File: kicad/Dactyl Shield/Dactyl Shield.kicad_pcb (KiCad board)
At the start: 4 copper layers, 99.4 x 91.3 mm, 130 parts, among them J201 JST, J202 Split, J203 Column, J205 Foot, J206 Row, J207 Display, J208 Vic, J209 ResA, J210 Thumb_row, J211 Thumb_upper, J212 ResB, J213 Thumb_lower, J301 JST, J302 Split, J303 Column, J305 Foot, J306 Row, J307 Display, J308 Vic, J309 ResA, J310 Thumb_row, J311 Thumb_upper, J312 ResB, J313 Thumb_lower, Q201 AO3400A, Q301 AO3400A, SW201 Battery, SW202 Reset, SW203 LED, SW301 Battery, SW302 Reset, SW303 LED, U201 SRV05-4, U202 Nice!Nano/2040, U301 SRV05-4, U302 Nice!Nano/2040

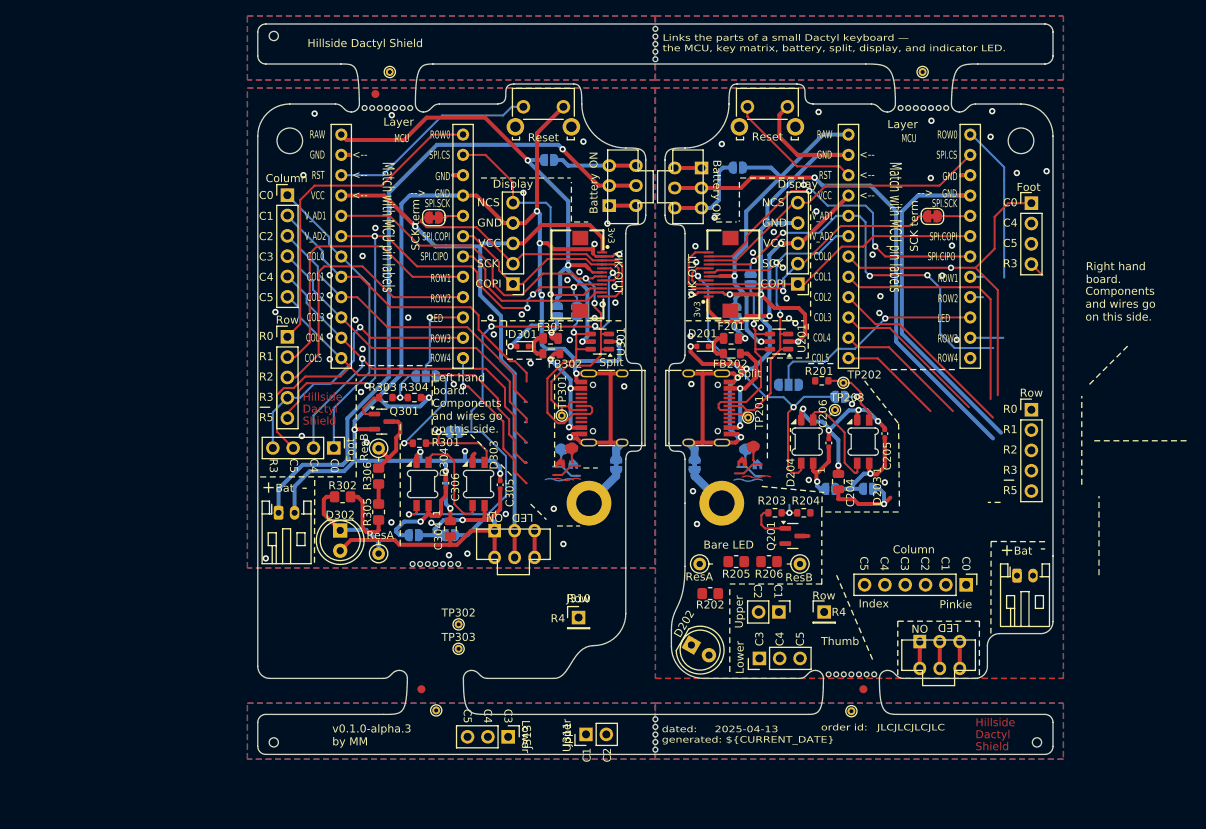
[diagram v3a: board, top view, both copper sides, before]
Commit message: feat: right side wired and seems good
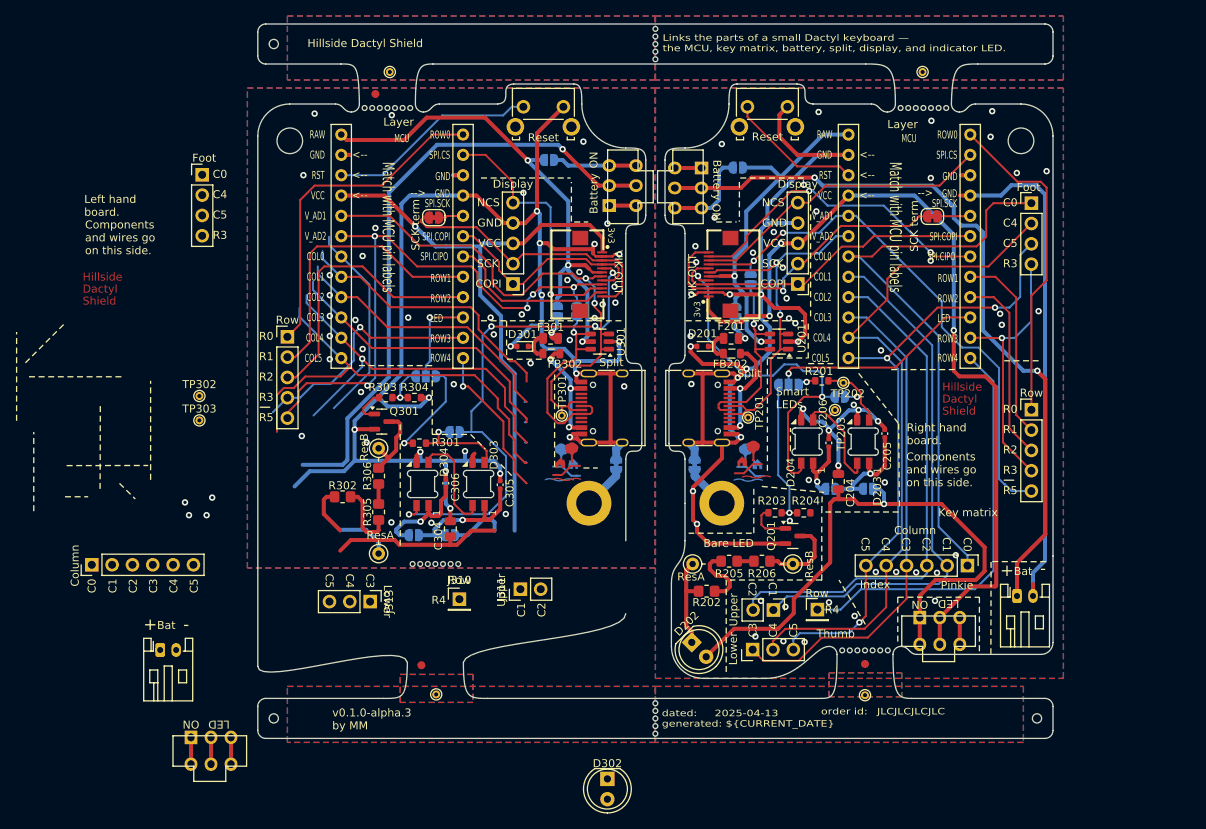
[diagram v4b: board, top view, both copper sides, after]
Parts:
- moved J303 52.3 mm to (69.0, 132.6), turned to 90 degrees
- moved SW303 45.9 mm to (84.0, 155.8)
- moved D302 45.6 mm to (133.5, 159.4)
- moved TP302 43.2 mm to (82.5, 111.5)
- moved TP303 43.2 mm to (82.5, 114.5)
- moved REF** 42.2 mm to (178.1, 112.0)
- moved J305 37.9 mm to (82.8, 83.8), turned to 0 degrees
- moved REF** 31.3 mm to (70.7, 98.2)
- moved J313 24.2 mm to (103.8, 137.2)
- moved J301 22.7 mm to (77.6, 143.2)
- moved J311 19.9 mm to (122.6, 135.7)
- moved J310 15.1 mm to (115.0, 136.9)
- moved REF** 3.45 mm to (165.7, 143.3)
- moved FID103 3.16 mm to (165.7, 145.0)
- moved FID102 3.00 mm to (110.2, 145.2)
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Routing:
- net /Right/VCC: track 31.2 -> 103.1 mm, vias 2 -> 3
- net /Right/col4: track 16.9 -> 86.6 mm
- net /Right/col5: track 13.0 -> 77.9 mm, vias 0 -> 3
- net /Right/VCC_LED: track 11.2 -> 70.1 mm
- net /Right/row4: track 0.22 -> 52.0 mm
- net /Right/GND: track 203.3 -> 251.1 mm, vias 46 -> 59
- net /Right/col3: track 19.7 -> 62.5 mm
- net /Right/col2: track 24.3 -> 64.4 mm
- net /Right/col1: track 31.4 -> 67.1 mm
- net /Right/bat+: track 60.0 -> 90.6 mm, vias 1 -> 2
- net /Right/row3: track 6.11 -> 33.8 mm, vias 0 -> 1
- net /Right/col0: track 46.2 -> 73.2 mm, vias 1 -> 0
- net /Right/row1: track 1.61 -> 24.2 mm
- net /Right/row2: track 1.61 -> 24.0 mm
- net /Right/row0: track 19.7 -> 40.8 mm
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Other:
- board size 99.4 x 91.3 mm -> 99.4 x 89.3 mm
- board text added: "Key matrix"
- board text added: "Smart LEDs"
